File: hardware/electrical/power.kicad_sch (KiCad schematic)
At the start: 4 parts, among them U101 AMS1117-3.3

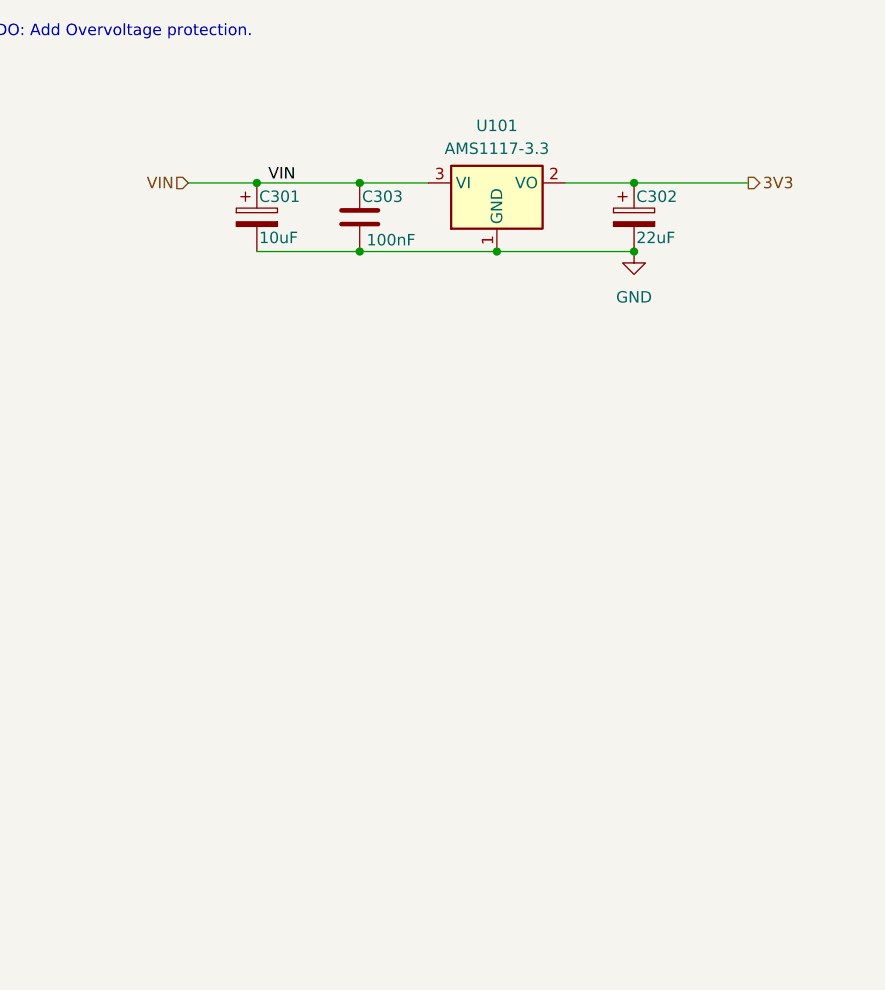
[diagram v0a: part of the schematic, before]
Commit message: (eda): add bq24072 chip for battery management and power delivery
begin schematic layout
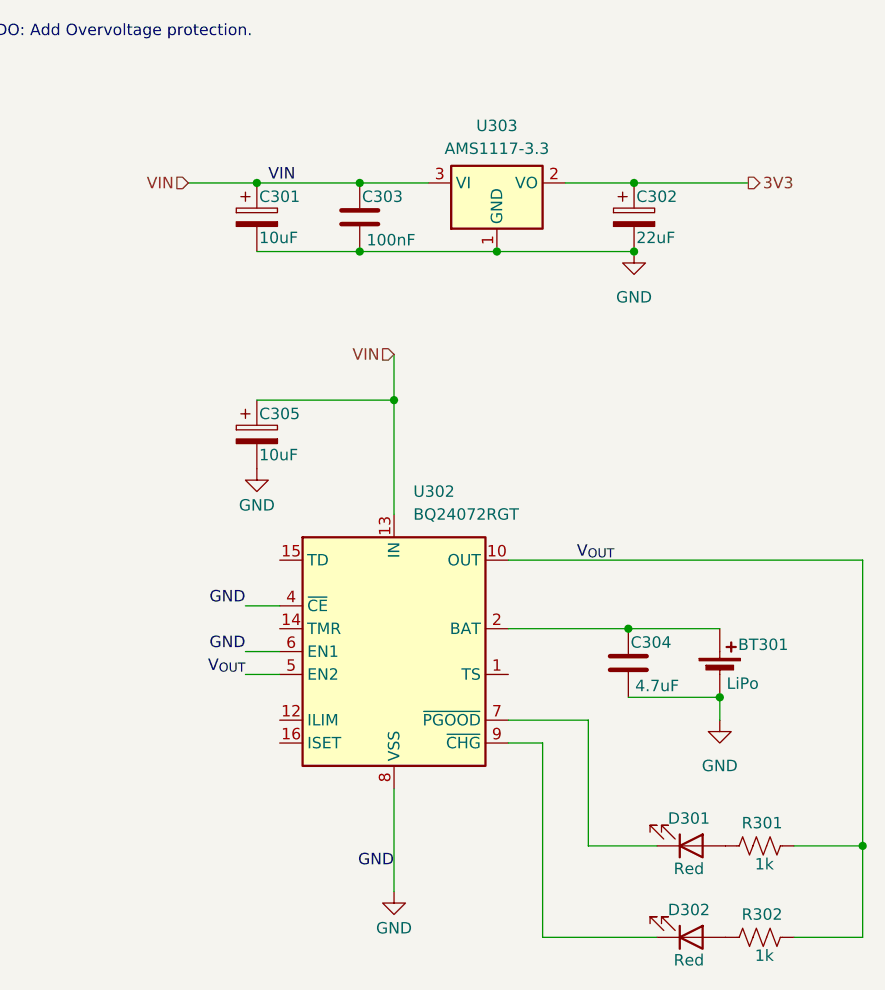
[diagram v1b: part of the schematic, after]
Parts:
- removed U101: AMS1117-3.3, Package_TO_SOT_SMD:SOT-223-3_TabPin2, symbol Regulator_Linear:AMS1117-3.3
- added BT301: LiPo, symbol Device:Battery_Cell
- added C304: 4.7uF, Capacitor_SMD:C_0402_1005Metric, symbol Device:C
- added C305: 10uF, Capacitor_Tantalum_SMD:CP_EIA-3216-18_Kemet-A, symbol Device:C_Polarized
- added D301, D302: Red, symbol Device:LED
- added R301, R302: 1k, symbol Device:R_US
- added U302: BQ24072RGT, Package_DFN_QFN:VQFN-16-1EP_3x3mm_P0.5mm_EP1.6x1.6mm, symbol Battery_Management:BQ24072RGT
- added U303: AMS1117-3.3, Package_TO_SOT_SMD:SOT-223-3_TabPin2, symbol Regulator_Linear:AMS1117-3.3
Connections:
- net 3V3: now also U303.2 (VO)
- net GND: now also BT301.2 (-), C304.2, C305.2, U302.17 (VSS), U302.4 (~{CE}), U302.6 (EN1), U302.8 (VSS), U303.1 (GND)
- net VIN: now also C305.1, U302.13 (IN), U303.3 (VI)
- new net: D302.1 (K), U302.9 (~{CHG})
- new net: D302.2 (A), R302.1
- new net: BT301.1 (+), C304.1, U302.2 (BAT), U302.3 (BAT)
- new net: D301.1 (K), U302.7 (~{PGOOD})
- new net: D301.2 (A), R301.1
- new net V_{OUT}: R301.2, R302.2, U302.10 (OUT), U302.11 (OUT), U302.5 (EN2)

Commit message: (eda): completed layout of bq24072
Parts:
- added R303, R304: 1.13k, symbol Device:R_US
- added TH301: 10k, Resistor_SMD:R_0603_1608Metric, symbol Device:Thermistor_NTC
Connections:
- net GND: now also U302.15 (TD), R303.1, R304.1, TH301.2
- net VIN: no longer C301.1, C303.1, U303.3 (VI)
- net V_{OUT}: no longer U302.10 (OUT), U302.11 (OUT)
- net ~{CHG}: now reaches D302.1 (K), U302.9 (~{CHG})
- net at U302.1 (TS): now also TH301.1
- net at U302.12 (ILIM): now also R303.2
- net at U302.16 (ISET): now also R304.2
- net ~{PGOOD}: now reaches D301.1 (K), U302.7 (~{PGOOD})
- new net: C301.1, C303.1, U302.10 (OUT), U302.11 (OUT), U303.3 (VI)
- no-connect marks 0 -> 1
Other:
- note added: "R_{ILIM} = K_{ILIM} / I_{I_MAX} K_{ILIM} = 1550Aohm"
- note added: "R_{ISET} = K_{ISET} / I_{CHG} K_{ISET} = 890Aohm"
- moved on the sheet: BT301, C301, C302, C303, C304, D301, D302, R301, R302, U303

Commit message: (eda): add switching buck converter from 12v to 5v
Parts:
- removed C301: 10uF, Capacitor_Tantalum_SMD:CP_EIA-3216-18_Kemet-A, symbol Device:C_Polarized
- removed C302: 22uF, Capacitor_Tantalum_SMD:CP_EIA-3216-18_Kemet-A, symbol Device:C_Polarized
- removed C303: 100nF, Capacitor_SMD:C_0402_1005Metric, symbol Device:C
- removed U303: AMS1117-3.3, Package_TO_SOT_SMD:SOT-223-3_TabPin2, symbol Regulator_Linear:AMS1117-3.3
- added C306, C310, C313: 100nF, Capacitor_SMD:C_0402_1005Metric, symbol Device:C
- added C307: 33nF, Capacitor_SMD:C_0402_1005Metric, symbol Device:C
- added C308, C309: 22uF, Capacitor_SMD:C_0402_1005Metric, symbol Device:C
- added C311, C312: 10uF, Capacitor_SMD:C_0402_1005Metric, symbol Device:C
- added L301: 6.8uH, symbol Device:L_Iron
- added R305: 52.5k, symbol Device:R_US
- added R306: 10k, symbol Device:R_US
- added U301: TPS62933, Package_TO_SOT_SMD:SOT-583-8, symbol Regulator_Switching:TPS62933
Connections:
- net GND: now also C307.2, C308.2, C309.2, C310.2, C311.2, C312.2, C313.2, R306.2, U301.4 (GND)
- net VIN renamed ${/42416d92-fe63-4085-b8a4-c2081c458f3d/ebc2fbdf-c059-4527-a940-510086278bcd/6f94f634-4532-4169-b1df-a711aecef6e3:Vout}
- net ${/42416d92-fe63-4085-b8a4-c2081c458f3d/ebc2fbdf-c059-4527-a940-510086278bcd/6f94f634-4532-4169-b1df-a711aecef6e3:Vout}: now also C308.1, C309.1, C310.1, L301.2, R305.2
- net ~{CHG} renamed ~{CHG}_{bat}
- net ~{PGOOD} renamed ~{PGOOD}_{bat}
- new net: C307.1, U301.7 (SS)
- new net: R305.1, R306.1, U301.8 (FB)
- new net: C306.1, U301.6 (BST)
- new net: C306.2, L301.1, U301.5 (SW)
- new net ${/42416d92-fe63-4085-b8a4-c2081c458f3d/ebc2fbdf-c059-4527-a940-510086278bcd/6f94f634-4532-4169-b1df-a711aecef6e3:Vin}: C311.1, C312.1, C313.1, U301.3 (VIN)
- no-connect marks 1 -> 3
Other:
- note added: "t_{SS} = C_{SS} * V_{REF} / I_{SS} Where: - t_{SS} is the soft start time. - V_{REF} is 0.8 V (the internal reference voltage). - I_{SS} is 5.5 μA (typical), the internal pullup current."
- note removed: "TODO: Add Overvoltage protection."
- moved on the sheet: BT301, C304, C305, D301, D302, R301, R302, R303, R304, TH301, U302

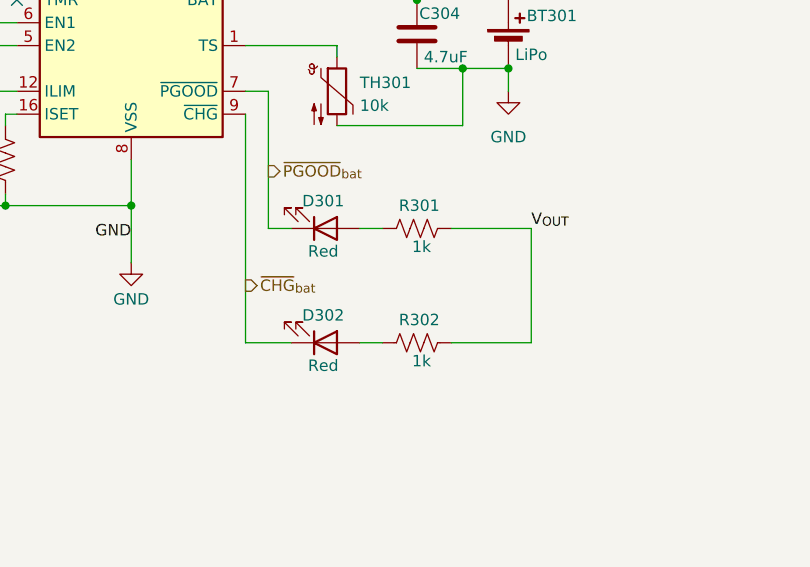
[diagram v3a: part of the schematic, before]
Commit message: (eda): mark leds and resistors as do not populate
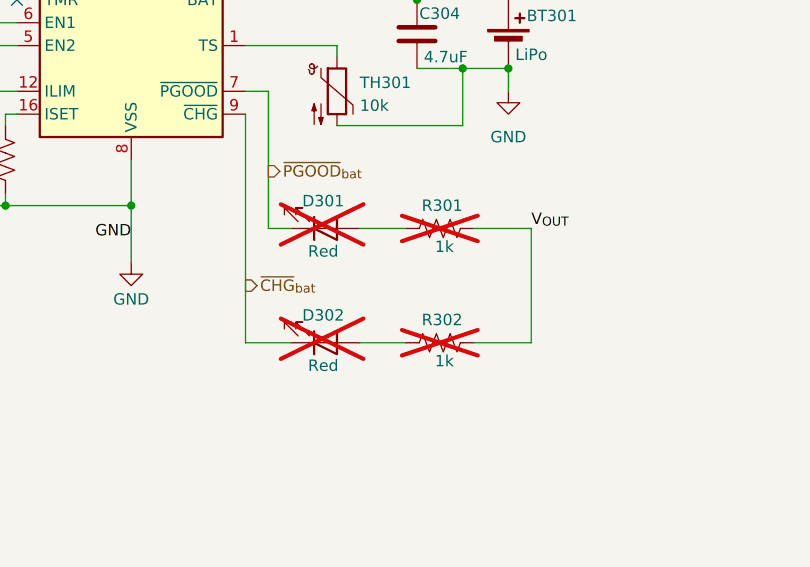
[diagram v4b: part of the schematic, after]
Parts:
- D301, D302, R301, R302: now not fitted
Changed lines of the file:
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@@
 	(wire
 		(pts
-			(xy 266.7 135.89) (xy 275.59 135.89)
+			(xy 269.24 135.89) (xy 275.59 135.89)
 		)
 		(stroke
@@
 	(wire
 		(pts
-			(xy 266.7 148.59) (xy 275.59 148.59)
+			(xy 269.24 148.59) (xy 275.59 148.59)
 		)
 		(stroke
@@
 	(wire
 		(pts
-			(xy 256.54 148.59) (xy 259.08 148.59)
+			(xy 256.54 148.59) (xy 261.62 148.59)
 		)
 		(stroke
@@
 	(wire
 		(pts
-			(xy 256.54 135.89) (xy 259.08 135.89)
+			(xy 256.54 135.89) (xy 261.62 135.89)
 		)
 		(stroke
@@
 		(in_bom yes)
 		(on_board yes)
-		(dnp no)
+		(dnp yes)
 		(property "Reference" "D302"
 			(at 252.476 145.542 0)
@@
 	(symbol
 		(lib_id "Device:R_US")
-		(at 262.89 135.89 90)
+		(at 265.43 135.89 90)
 		(unit 1)
 		(exclude_from_sim no)
 		(in_bom yes)
 		(on_board yes)
-		(dnp no)
+		(dnp yes)
 		(property "Reference" "R301"
-			(at 263.144 133.35 90)
+			(at 265.684 133.35 90)
 			(effects
 				(font
@@
 		)
 		(property "Value" "1k"
-			(at 263.398 137.922 90)
+			(at 265.938 137.922 90)
 			(effects
 				(font
@@
 		)
 		(property "Footprint" ""
-			(at 263.144 134.874 90)
+			(at 265.684 134.874 90)
 			(effects
 				(font
@@
 		)
 		(property "Datasheet" "~"
-			(at 262.89 135.89 0)
+			(at 265.43 135.89 0)
 			(effects
 				(font
@@
 		)
 		(property "Description" "Resistor, US symbol"
-			(at 262.89 135.89 0)
+			(at 265.43 135.89 0)
 			(effects
 				(font
@@
 	(symbol
 		(lib_id "Device:R_US")
-		(at 262.89 148.59 90)
+		(at 265.43 148.59 90)
 		(unit 1)
 		(exclude_from_sim no)
 		(in_bom yes)
 		(on_board yes)
-		(dnp no)
+		(dnp yes)
 		(property "Reference" "R302"
-			(at 263.144 146.05 90)
+			(at 265.684 146.05 90)
 			(effects
 				(font
@@
 		)
 		(property "Value" "1k"
-			(at 263.398 150.622 90)
+			(at 265.938 150.622 90)
 			(effects
 				(font
@@
 		)
 		(property "Footprint" ""
-			(at 263.144 147.574 90)
+			(at 265.684 147.574 90)
 			(effects
 				(font
@@
 		)
 		(property "Datasheet" "~"
-			(at 262.89 148.59 0)
+			(at 265.43 148.59 0)
 			(effects
 				(font
@@
 		)
 		(property "Description" "Resistor, US symbol"
-			(at 262.89 148.59 0)
+			(at 265.43 148.59 0)
 			(effects
 				(font
@@
 		(in_bom yes)
 		(on_board yes)
-		(dnp no)
+		(dnp yes)
 		(property "Reference" "D301"
 			(at 252.476 132.842 0)
